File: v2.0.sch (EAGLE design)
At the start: 235 parts, among them J1 DC-044-A, J10 16p-2.54, J11 16p-2.54, J12 4p-2.54, J2 MICROSD-9P, J3 2p-2.54, J4 2p-2.54, J5 16p-2.54, J6 16p-2.54, J7 16p-2.54, J9 16p-2.54, Q1 32.768khZ@6Pf, Q10 S8550, Q2 SSM3J328R,LF, Q3 BSS138W-7-F, Q4 BSS138W-7-F, Q5 SSM3J328R,LF, Q6 BSS138W-7-F, Q7 BSS138W-7-F, Q8 CJ2305, Q9 S8550, SW1 MK-12C02 G1.5, SW2 MK-12C02 G1.5, SW3 MK-12C02 G1.5, SW4 MK-12C02 G1.5, U1 MCP23017-E/SO, U10 74HCT139D, U11 BZX84C30, U12 SP483ECN-L, U13 FT232RL-SSOP28, U14 FT232RL-SSOP28, U15 FT232RL-SSOP28, U2 MCP79412-I/SN, U3 LOPY, U4 MAX213IDBR, U5 FT232RL-SSOP28, U8 BR24G32-3, Y2 12MHZ

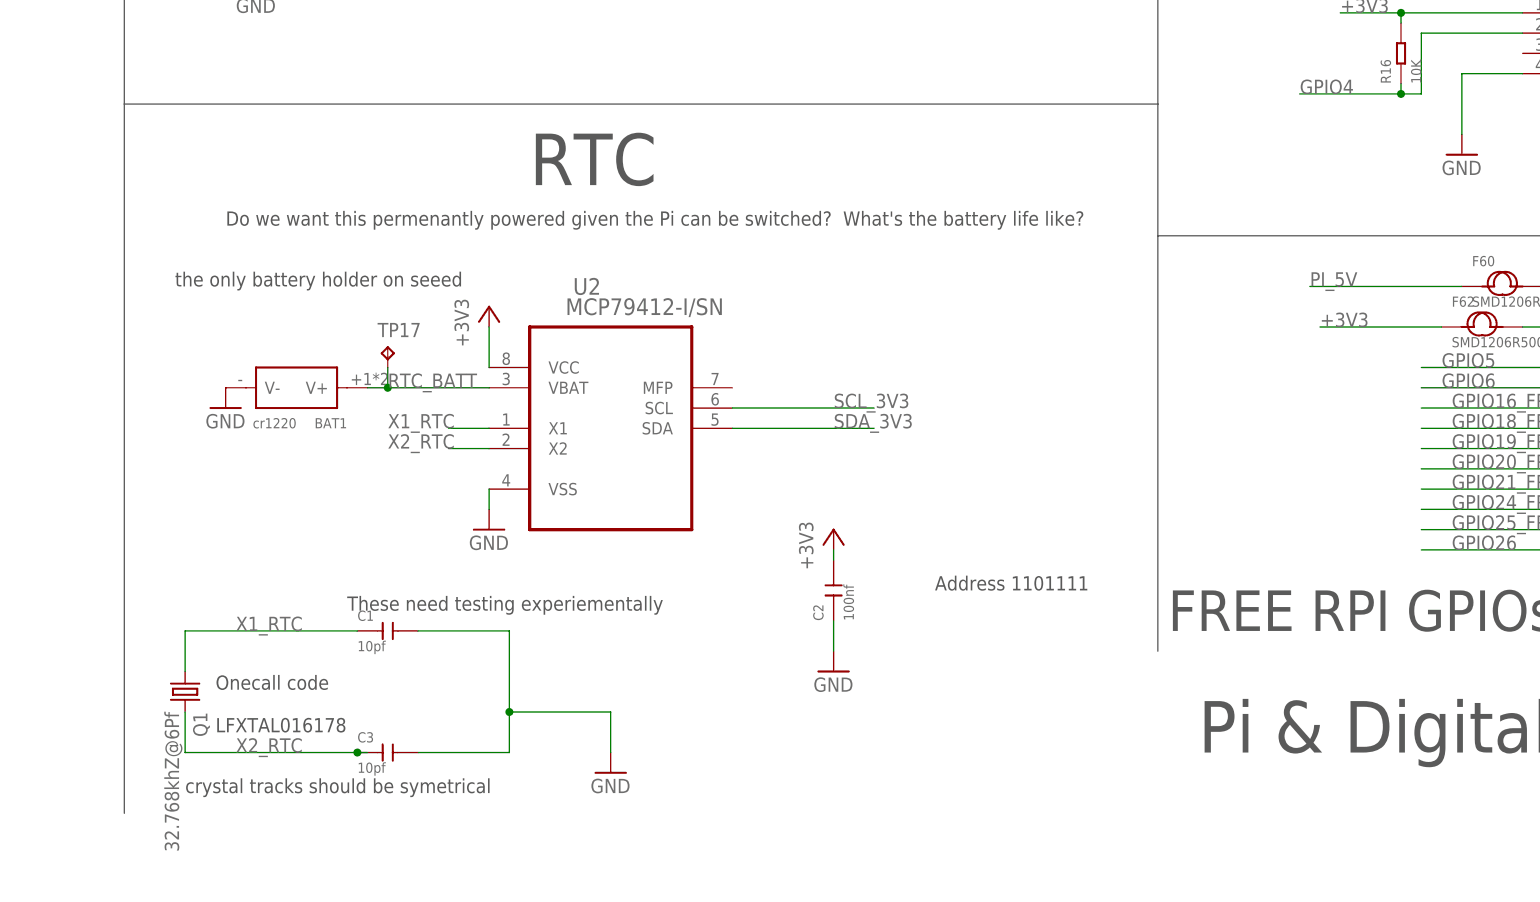
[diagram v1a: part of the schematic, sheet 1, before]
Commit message: RTC changed to one that doesn't rely on external crystal
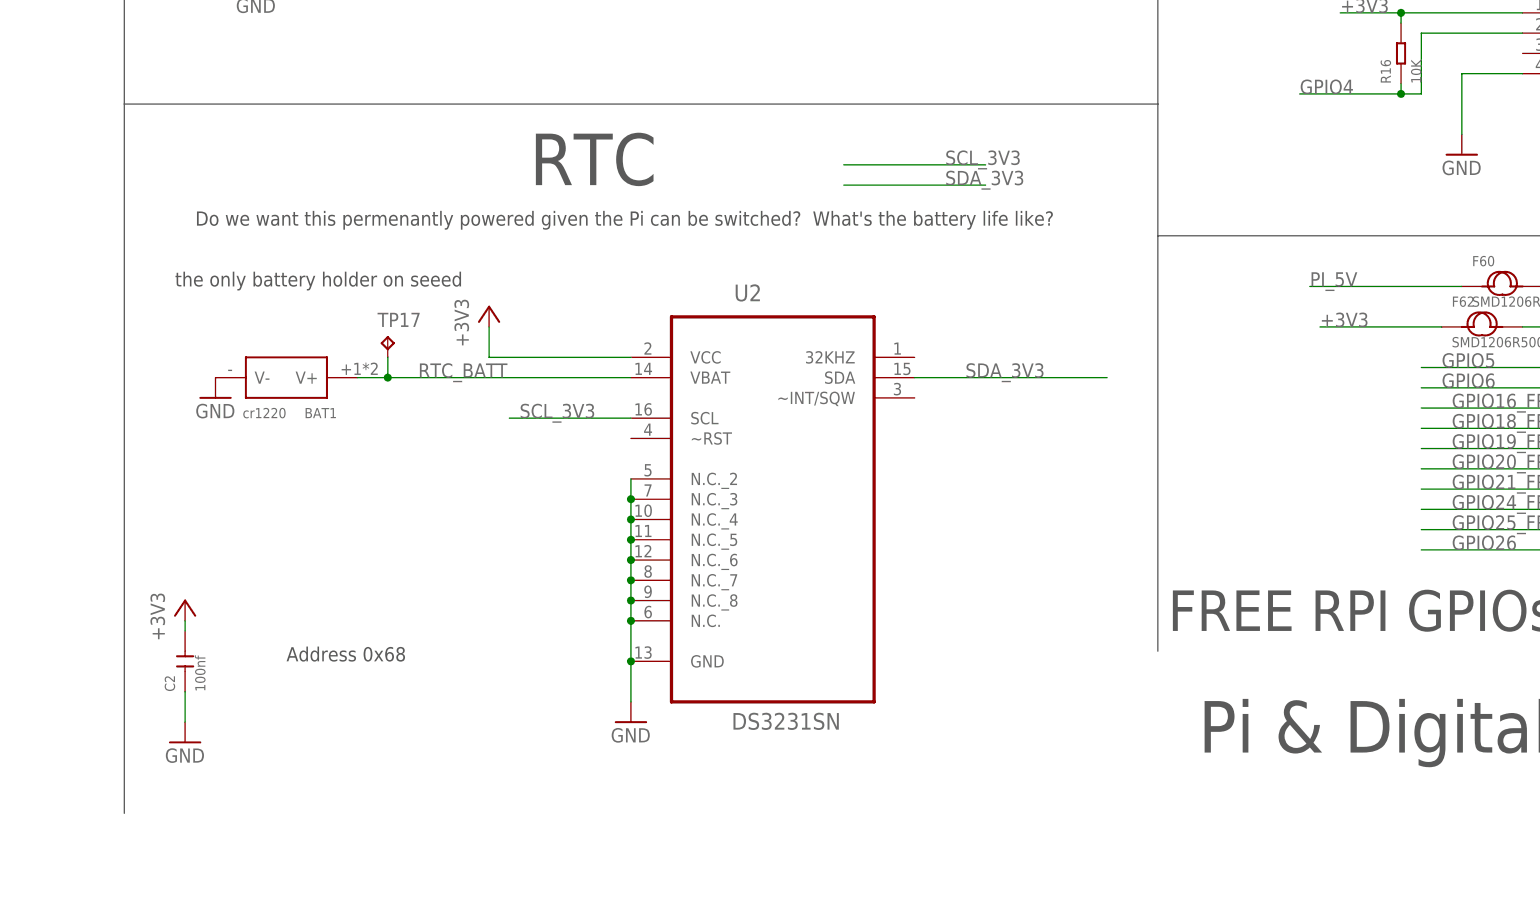
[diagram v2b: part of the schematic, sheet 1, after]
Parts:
- removed C1, C3: 10pf, Seeed-Capacitor:CERAMIC-10PF-50V-5%-NPO(0603)
- removed Q1: 32.768khZ@6Pf, imported-parts:LFXTAL016178
- added JP2: (no value), jumper:JP1E
- U2: value MCP79412-I/SN -> DS3231SN; device imported-parts:MCP79412-I/SN -> imported-parts:DS3231SN
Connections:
- removed net X1_RTC: C1.1, Q1.1, U2.X1
- removed net X2_RTC: C3.1, Q1.2, U2.X2
- net GND: now also JP2.1, JP2.2, U2.GND, U2.N.C., U2.N.C._2, U2.N.C._3, U2.N.C._4, U2.N.C._5, U2.N.C._6, U2.N.C._7, U2.N.C._8; no longer C1.2, C3.2, U2.VSS
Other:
- note added: "Address 0x68"
- note added: "For test loop for probes"
- note removed: "Address 1101111"
- note removed: "Onecall code LFXTAL016178"
- note removed: "These need testing experiementally"
- note removed: "crystal tracks should be symetrical"
- moved on the sheet: BAT1, C2, TP17

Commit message: More layout tweaking
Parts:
- added PI_UART_HUB_1: JST-XH-05-PIN-ROUND-PAD, Rembrandt Electronics - JST XH Connectors v1-0 2:JST-XH-05-PIN-ROUND-PAD
- added R1, R3: 0R, Seeed-Resistor:SMD-RES-0R-5%-1/10W(0603)
- added R11, R13: DNP, rcl:R-EU_R0603
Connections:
- new net RXD3_CONV: R13.1, U4.ROUT3
- new net TTL3_OUT_RXD: PI_UART_HUB_1-4.S, R3.2
- new net TTL3_OUT_TXD: PI_UART_HUB_1-3.S, R1.2
- new net TXD3_CONV: R11.1, U4.DIN3
- net GND: now also PI_UART_HUB_1-5.S
- net RXD3: now also R13.2, R3.1; no longer U4.ROUT3
- net TXD3: now also R1.1, R11.2; no longer U4.DIN3
- net UART_HUB_3_3V3_P: now also PI_UART_HUB_1-2.S
- net UART_USB_HUB_3_5V: now also PI_UART_HUB_1-1.S
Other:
- moved on the sheet: F10, F15, F16, F19, F20, F40, F41, F42, F43, F5, F6, F9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
